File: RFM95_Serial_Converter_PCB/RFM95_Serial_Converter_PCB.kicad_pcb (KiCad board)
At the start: 2 copper layers, 43 parts, among them J1 Conn_01x04, J2 SM06B-GHS-TB(LF)(SN), J3 SM06B-GHS-TB(LF)(SN), J4 USB_B_Micro, J5 USB_B_Micro, SW1 SW_Push, SW2 SW_Push, U1 RFM95W-915S2, U2 AMS1117-3.3, U3 USBLC6-2SC6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

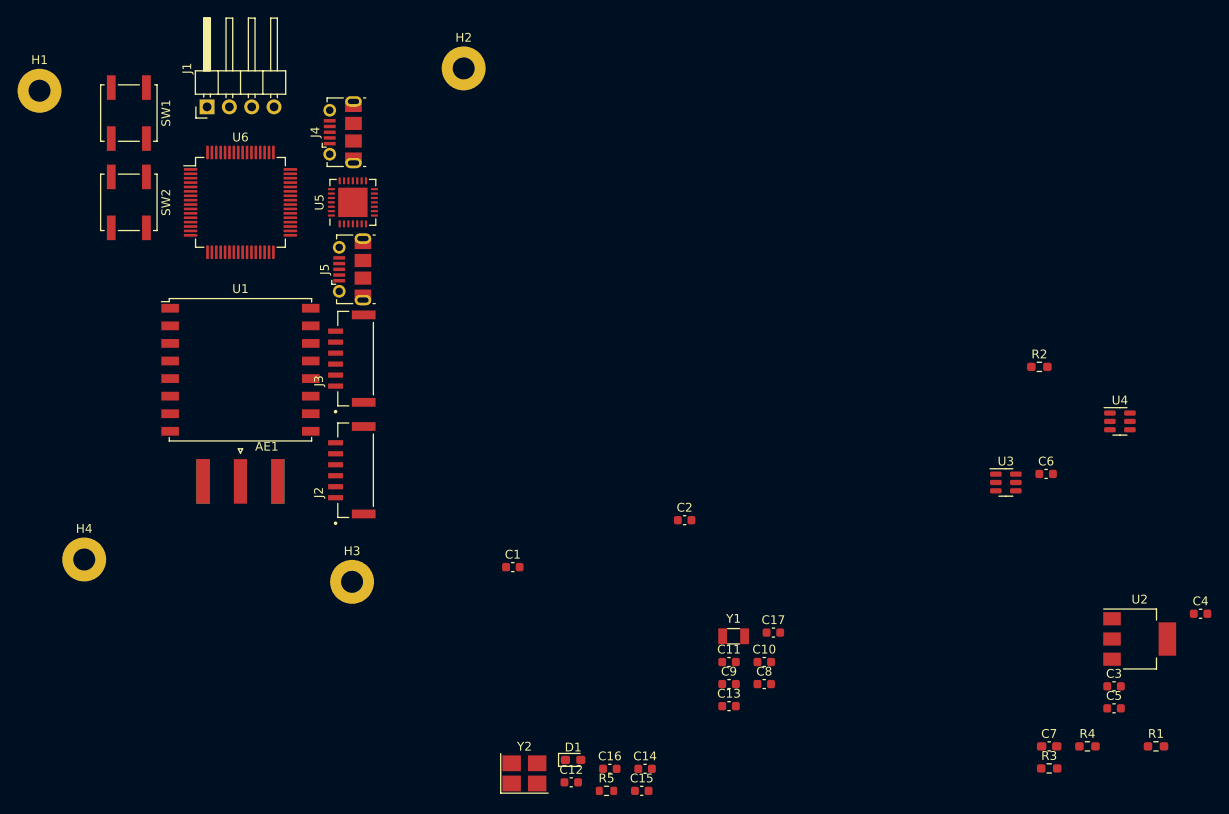
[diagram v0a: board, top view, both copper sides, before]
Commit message: Finalised component placement and board edge
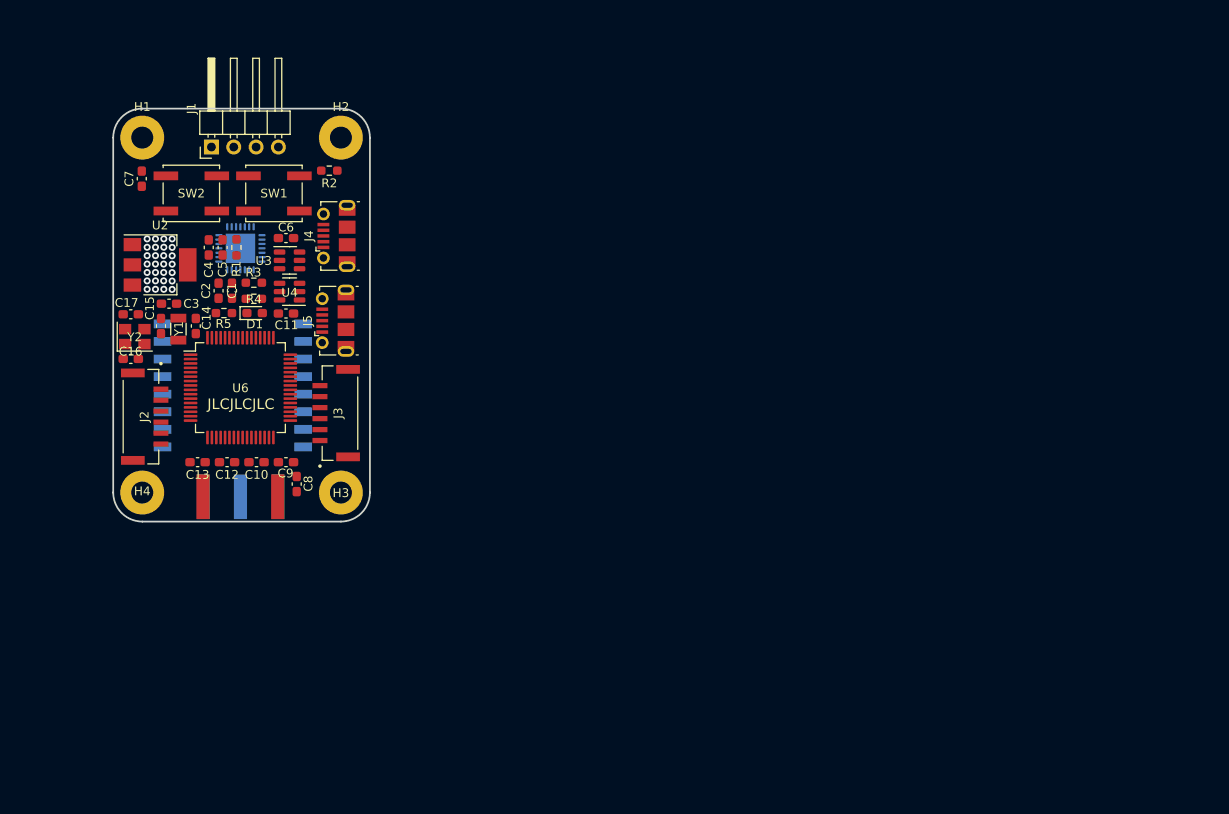
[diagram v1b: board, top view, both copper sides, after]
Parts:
- AE1, U1, U5: moved to B.Cu
- C1, C10, C11, C12, C13, C14, C15, C16, C17, C2, C3, C4, C5, C6, C8, C9: footprint Capacitor_SMD:C_0603_1608Metric -> Capacitor_SMD:C_0603_1608Metric_Pad1.08x0.95mm_HandSolder
- R5: footprint Resistor_SMD:R_0603_1608Metric -> Resistor_SMD:R_0603_1608Metric_Pad0.98x0.95mm_HandSolder
- Y2: footprint Crystal:Crystal_SMD_3225-4Pin_3.2x2.5mm_HandSoldering -> Crystal:Crystal_SMD_3225-4Pin_3.2x2.5mm
- moved C7 121.8 mm to (65.0, 48.1), turned to 90 degrees
- moved C4 120.3 mm to (72.6, 55.9), turned to 90 degrees
- moved U2 119.3 mm to (67.1, 57.9)
- moved R1 119.0 mm to (75.7, 55.9), turned to 90 degrees
- moved C3 116.0 mm to (68.1, 62.3)
- moved C5 114.2 mm to (74.2, 55.9), turned to 90 degrees
- moved R4 107.7 mm to (77.7, 61.8), turned to 180 degrees
- moved R3 106.0 mm to (77.7, 59.9), turned to 180 degrees
- moved U4 95.6 mm to (81.8, 61.0), turned to 180 degrees
- moved C6 90.6 mm to (81.4, 54.9)
- moved U3 85.3 mm to (81.8, 57.4)
- moved R2 83.8 mm to (86.3, 47.2), turned to 180 degrees
- moved C17 81.6 mm to (63.7, 63.5), turned to 180 degrees
- moved C15 76.1 mm to (67.2, 64.9), turned to 90 degrees
- moved Y1 72.2 mm to (69.1, 65.2), turned to 90 degrees
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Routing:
- net (no net): vias 0 -> 28
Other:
- board outline added: 29.2 x 47 mm
- board text added: "JLCJLCJLC"

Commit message: Routed and ready to order
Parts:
- moved U5 1.22 mm to (75.0, 56.0)
- moved J3 0.87 mm to (87.8, 75.3)
- moved J2 0.47 mm to (64.8, 75.3)
- moved J1 0.38 mm to (72.5, 44.5)
- moved J5 0.36 mm to (87.3, 64.3)
- moved U6 0.24 mm to (76.3, 72.1)
- moved J4 0.23 mm to (87.3, 54.6)
- moved C8 0.20 mm to (82.8, 82.9)
- moved AE1 0.13 mm to (76.3, 84.3)
- turned U3 to 180 degrees
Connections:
- net Net-(J4-Pad2) renamed /Data_Interfaces/USB1_D-
- net Net-(J4-Pad3) renamed /Data_Interfaces/USB1_D+
- net Net-(J5-Pad2) renamed /Data_Interfaces/USB2_D-
- net Net-(J5-Pad3) renamed /Data_Interfaces/USB2_D+
- net Net-(R3-Pad2) renamed /STM32F405/USB2_IN-
- net Net-(R4-Pad2) renamed /STM32F405/USB2_IN+
- net Net-(U3-Pad4) renamed /Data_Interfaces/USB1_IN_D-
- net Net-(U3-Pad6) renamed /Data_Interfaces/USB1_IN_D+
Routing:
- net +5V: track 0.00 -> 59.9 mm, vias 0 -> 1
- net +3V3: track 0.00 -> 50.1 mm, vias 0 -> 17
- net GND: track 0.00 -> 48.1 mm, vias 0 -> 77
- net /Data_Interfaces/RX_RADIO: track 0.00 -> 42.6 mm, vias 0 -> 3
- net /Data_Interfaces/CTS_RADIO: track 0.00 -> 40.3 mm, vias 0 -> 3
- net Net-(C7-Pad2): track 0.00 -> 36.1 mm, vias 0 -> 2
- net Net-(R2-Pad2): track 0.00 -> 36.0 mm, vias 0 -> 2
- net /Data_Interfaces/RTS_RADIO: track 0.00 -> 32.7 mm, vias 0 -> 3
- net /Data_Interfaces/SWDIO: track 0.00 -> 29.2 mm, vias 0 -> 1
- net /Data_Interfaces/TX_RADIO: track 0.00 -> 27.5 mm, vias 0 -> 1
- net /Data_Interfaces/SWCLK: track 0.00 -> 25.5 mm, vias 0 -> 1
- net /915MHz_Radio/IO2_RF: track 0.00 -> 20.9 mm, vias 0 -> 1
- net /STM32F405/USB2_IN-: track 0.00 -> 19.1 mm, vias 0 -> 2
- net /STM32F405/USB2_IN+: track 0.00 -> 19.0 mm, vias 0 -> 2
- net /915MHz_Radio/IO1_RF: track 0.00 -> 18.4 mm, vias 0 -> 1
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- added copper zone on In2.Cu, net +3V3
- added copper zone on B.Cu, net GND
- added copper zone on F.Cu, net GND
- added copper zone on In1.Cu, net GND
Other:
- copper layers 2 -> 4

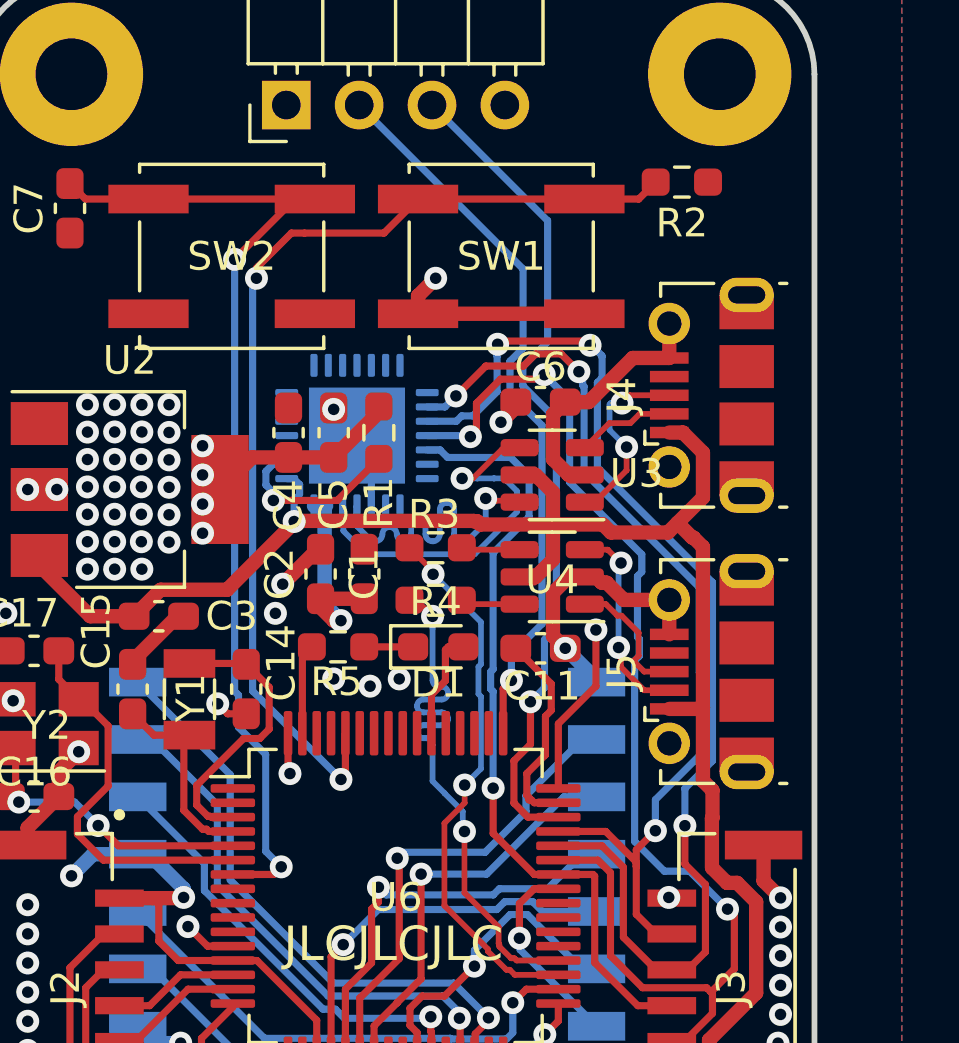
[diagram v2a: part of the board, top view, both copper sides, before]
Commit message: Repositioned indicator led and exported step
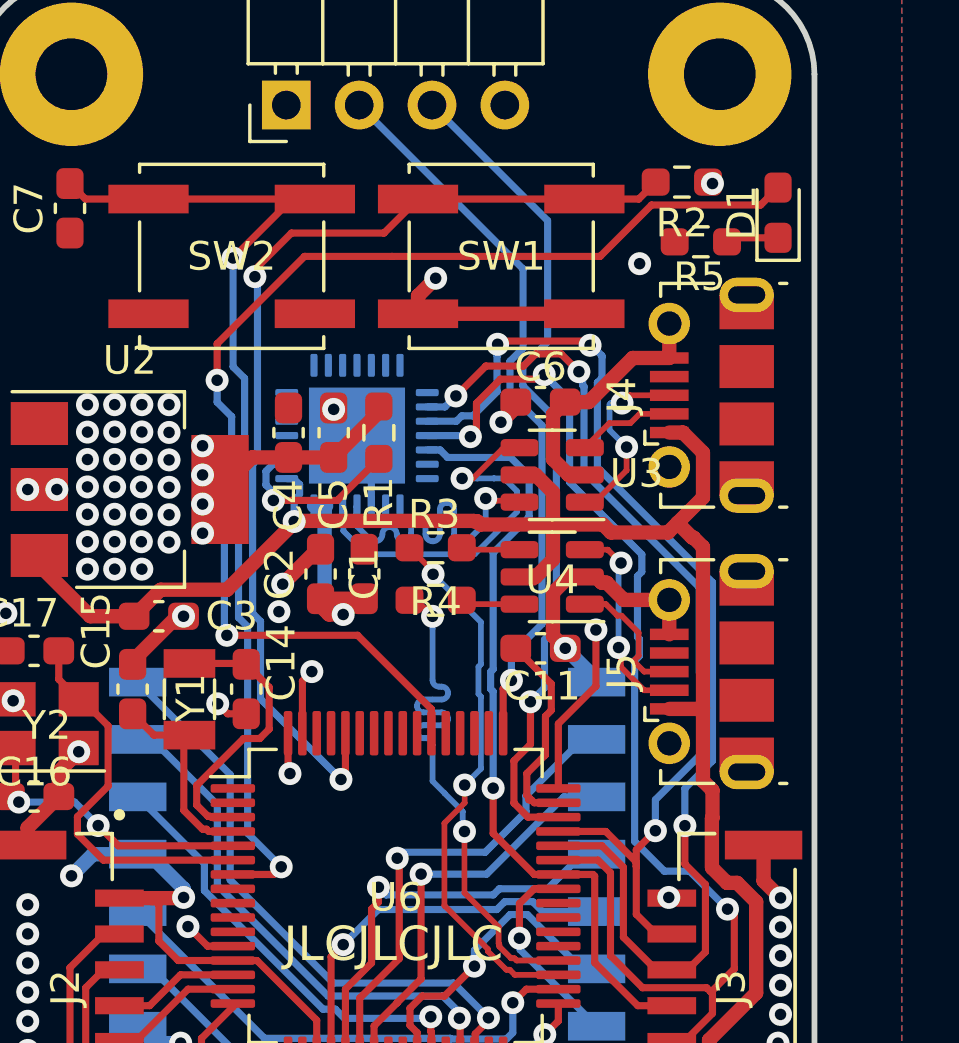
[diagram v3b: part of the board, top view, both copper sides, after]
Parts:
- D1: value BLUE_LED -> E6X0602QBAC1UDA
- moved D1 19.2 mm to (89.7, 48.3), turned to 90 degrees
- moved R5 19.0 mm to (87.0, 49.3)
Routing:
- net /STM32F405/INDICATOR_LED: track 3.78 -> 41.4 mm, vias 0 -> 2
- net GND: track 48.1 -> 47.2 mm, vias 77 -> 78

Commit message: Working verison of code
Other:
- board text added: "Designed by Angus McLennan Jun 2022"
- board text added: "RFM95 3DR"
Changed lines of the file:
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@@
     (property "Sheetname" "Data_Interfaces")
     (attr through_hole)
-    (fp_text reference "J1" (at 4.385 -2.27 90) (layer "F.SilkS")
+    (fp_text reference "J1" (at 2.77 3.81) (layer "F.SilkS")
       (effects (font (size 1 1) (thickness 0.15)))
     )
@@
     (property "Sheetname" "")
     (attr exclude_from_pos_files)
-    (fp_text reference "H2" (at 0 -3.5) (layer "F.SilkS")
+    (fp_text reference "H2" (at 0 -4.318) (layer "F.SilkS")
       (effects (font (size 1 1) (thickness 0.15)))
     )
@@
     (property "Sheetname" "")
     (attr exclude_from_pos_files)
-    (fp_text reference "H1" (at 0 -3.5) (layer "F.SilkS")
+    (fp_text reference "H1" (at 0 -4.318) (layer "F.SilkS")
       (effects (font (size 1 1) (thickness 0.15)))
     )
@@
   (gr_arc (start 61.722 43.434) (mid 62.689133 41.099133) (end 65.024 40.132) (layer "Edge.Cuts") (width 0.2))
   (gr_arc (start 87.63 40.132) (mid 89.964867 41.099133) (end 90.932 43.434) (layer "Edge.Cuts") (width 0.2))
+  (gr_text "Designed by\nAngus McLennan\nJun 2022" (at 82.804 60.96) (layer "B.SilkS")
+    (effects (font (size 0.8 0.8) (thickness 0.2)) (justify left mirror))
+  )
+  (gr_text "RFM95 3DR" (at 76.2 48.26) (layer "B.SilkS")
+    (effects (font (size 2 2) (thickness 0.3)) (justify mirror))
+  )
   (gr_text "JLCJLCJLC" (at 76.2508 73.7616) (layer "F.SilkS")
     (effects (font (size 1.2 1.2) (thickness 0.3)))
